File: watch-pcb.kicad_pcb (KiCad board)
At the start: 6 copper layers, 43 x 43 mm, 158 parts, among them J1 DAUGHTER, J2 USB_C_Receptacle, J3 Micro_SD_Card, J4 ELV1411A, J6 TT143AMC12C, U1 ADP2108AUJ-1.8, U10 MAX30102, U11 TPS65631W, U13 LSM6DSV16XTR, U14 LIS3MDL, U15 TXS02612RTW, U16 DRV2605LDGS, U2 TPS63021, U3 STM32H7S7L8H6H, U4 BQ27427YZFR, U5 APS256XXN-OBR-BG, U6 BQ25628E, U7 MX25LM51245GXDI00, U8 APS12808L-3OBMx, U9 TCA9535MRGER, Y1 32.768kHz, Y2 40MHz(10ppm), Y3 32.768kHz, Y4 40MHz(10ppm)

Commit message: no more daughter probably
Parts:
- removed C104, C106: 1uF, Capacitor_SMD:C_0402_1005Metric
- removed C105: 100nF, Capacitor_SMD:C_0402_1005Metric
- removed C52, C89, C90: 10uF, Capacitor_SMD:C_0402_1005Metric
- removed C88: 4.7uF, Capacitor_SMD:C_0402_1005Metric
- removed J4: ELV1411A, custom-lib:ELV1411A
- removed R36, R37: 0, Resistor_SMD:R_0402_1005Metric
- removed R52, R53, R54: 10k, Resistor_SMD:R_0402_1005Metric
- removed R55, R56, R57: R, Resistor_SMD:R_0402_1005Metric
- removed R60: 30.1, Resistor_SMD:R_0402_1005Metric
- removed R61: 5.32k, Resistor_SMD:R_0402_1005Metric
- removed R62: 5k, Resistor_SMD:R_0402_1005Metric
- removed TH2: 103AT-2 10k, Resistor_SMD:R_0603_1608Metric
- removed Y3: 32.768kHz, Crystal:Crystal_SMD_3215-2Pin_3.2x1.5mm
- removed Y4: 40MHz(10ppm), Crystal:Crystal_SMD_3225-4Pin_3.2x2.5mm
- added C19: 1uF, Capacitor_SMD:C_0402_1005Metric, F.Cu at (172.2, 91.1)
- added C20: 2.2uF, Capacitor_SMD:C_0402_1005Metric, F.Cu at (172.2, 93.1)
- added C23: 1uF, Capacitor_SMD:C_0402_1005Metric, F.Cu at (155.5, 56.0)
- added C24: 100nF, Capacitor_SMD:C_0402_1005Metric, F.Cu at (155.5, 57.9)
- added C25: 100nF, Capacitor_SMD:C_0402_1005Metric, F.Cu at (155.5, 59.9)
- added C29: 100nF, Capacitor_SMD:C_0402_1005Metric, F.Cu at (155.5, 67.8)
- added C34: 1uF, Capacitor_SMD:C_0402_1005Metric, F.Cu at (158.4, 63.9)
- added C37: 100nF, Capacitor_SMD:C_0402_1005Metric, F.Cu at (161.2, 56.0)
- added C53: 100nF, Capacitor_SMD:C_0402_1005Metric, F.Cu at (138.6, 55.2)
- added C56: 100nF, Capacitor_SMD:C_0402_1005Metric, F.Cu at (141.5, 45.4)
- added C80: 10uF, Capacitor_SMD:C_0805_2012Metric, F.Cu at (198.9, 91.3)
- added C81: 100nF, Capacitor_SMD:C_0402_1005Metric, F.Cu at (132.2, 95.7)
- added C82: 1uF, Capacitor_SMD:C_0402_1005Metric, F.Cu at (132.2, 97.7)
- added D10: ESD9B3.3ST5G, Diode_SMD:D_SOD-923, F.Cu at (150.1, 47.3)
- added D11: ESD9B3.3ST5G, Diode_SMD:D_SOD-923, F.Cu at (150.1, 49.3)
- added D12: ESD9B3.3ST5G, Diode_SMD:D_SOD-923, F.Cu at (150.1, 51.2)
- added D13: ESD9B3.3ST5G, Diode_SMD:D_SOD-923, F.Cu at (150.1, 53.2)
- added D14: ESD9B3.3ST5G, Diode_SMD:D_SOD-923, F.Cu at (150.1, 55.1)
- added D17: APFA3010, LED_SMD:LED_Kingbright_APFA3010_3x1.5mm_Horizontal, F.Cu at (158.0, 137.2)
- added D8: ESD9B5.0ST5G, Diode_SMD:D_SOD-923, F.Cu at (175.2, 81.0)
- added D9: ESD9B3.3ST5G, Diode_SMD:D_SOD-923, F.Cu at (150.1, 45.4)
- added J5: Micro_SD_Card, Connector_Card:microSD_HC_Molex_104031-0811, F.Cu at (112.4, 163.6)
- added L3: 2.2uH, Inductor_SMD:L_1206_3216Metric, F.Cu at (126.5, 177.0)
- added L4: 2.7nH, Inductor_SMD:L_0201_0603Metric, F.Cu at (178.5, 48.8)
- added R17: 5.1k, Resistor_SMD:R_0402_1005Metric, F.Cu at (166.4, 91.2)
- added R18: 10k, Resistor_SMD:R_0402_1005Metric, F.Cu at (166.4, 93.1)
- added R20: 10k, Resistor_SMD:R_0402_1005Metric, F.Cu at (167.0, 58.0)
- added R21: R, Capacitor_SMD:C_0402_1005Metric, F.Cu at (198.1, 95.8)
- added R22: 10k, Resistor_SMD:R_0402_1005Metric, F.Cu at (167.0, 60.0)
- added R23: 10k, Resistor_SMD:R_0402_1005Metric, F.Cu at (167.0, 62.0)
- added R24: 10k, Resistor_SMD:R_0402_1005Metric, B.Cu at (223.9, 75.6)
- added R25: 499, Resistor_SMD:R_0402_1005Metric, F.Cu at (169.9, 58.0)
- added R26: 0, Resistor_SMD:R_0402_1005Metric, F.Cu at (169.9, 60.0)
- added R27: 0, Resistor_SMD:R_0402_1005Metric, F.Cu at (169.9, 62.0)
- added R28: 0, Resistor_SMD:R_0402_1005Metric, F.Cu at (172.8, 56.0)
- added R29: 0, Resistor_SMD:R_0402_1005Metric, F.Cu at (172.8, 58.0)
- added R30: 0, Resistor_SMD:R_0402_1005Metric, F.Cu at (172.8, 60.0)
- added R46: 10k, Resistor_SMD:R_0402_1005Metric, F.Cu at (141.6, 69.1)
- added TH1: 103AT-2 10k, Resistor_SMD:R_0603_1608Metric, F.Cu at (119.1, 169.5)
- added U12: LSM6DSOXTR, Package_LGA:LGA-14_3x2.5mm_P0.5mm_LayoutBorder3x4y, F.Cu at (125.6, 155.6)
- added U17: KTD2026, Package_DFN_QFN:DFN-8-1EP_1.5x1.5mm_P0.4mm_EP0.7x1.2mm, F.Cu at (120.9, 106.1)
- C1: value 10uF -> 1uF; footprint Capacitor_SMD:C_0603_1608Metric -> Capacitor_SMD:C_0402_1005Metric; moved to F.Cu
- C10: moved to B.Cu
- C11: value 1uF -> 22uF; footprint Capacitor_SMD:C_0402_1005Metric -> Capacitor_SMD:C_0603_1608Metric; moved to B.Cu
- C12: value 100nF -> 4.7uF; footprint Capacitor_SMD:C_0402_1005Metric -> Capacitor_SMD:C_0603_1608Metric; moved to F.Cu
- C13: footprint Capacitor_SMD:C_0402_1005Metric -> Capacitor_SMD:C_0603_1608Metric; moved to F.Cu
- C14: value 1uF -> 10uF; footprint Capacitor_SMD:C_0402_1005Metric -> Capacitor_SMD:C_0603_1608Metric; moved to F.Cu
- C15: value 2.2uF -> 10uF; footprint Capacitor_SMD:C_0402_1005Metric -> Capacitor_SMD:C_0805_2012Metric
- C16: value 47nF -> 10uF; footprint Capacitor_SMD:C_0402_1005Metric -> Capacitor_SMD:C_0603_1608Metric; moved to F.Cu
- C17: value 100nF -> 22uF; footprint Capacitor_SMD:C_0402_1005Metric -> Capacitor_SMD:C_0603_1608Metric; moved to F.Cu
- C18: value 1uF -> 10nF; moved to F.Cu
- C2: value 10uF -> 100nF; footprint Capacitor_SMD:C_0603_1608Metric -> Capacitor_SMD:C_0402_1005Metric; moved to F.Cu
- C21, C22: value C -> 1.5pF; footprint Capacitor_SMD:C_0402_1005Metric -> Capacitor_SMD:C_0201_0603Metric
- C26, C45, C66: value 1uF -> 100nF; moved to F.Cu
- C27, C41: value C -> 1uF
- C28, C42: value C -> 100nF
- C3: value 4.7uF -> 10uF; footprint Capacitor_SMD:C_0402_1005Metric -> Capacitor_SMD:C_0603_1608Metric; moved to F.Cu
- C30, C38, C70, D3, L5, L7, L8, R44: moved to F.Cu
- C31, C47: value 1uF -> C
- C32: value 100nF -> C; moved to F.Cu
- C33: value 1uF -> 10nF
- C36: value 10nF -> 1uF
- C39, C48: value 100nF -> 1uF; moved to F.Cu
- C4: footprint Capacitor_SMD:C_0603_1608Metric -> Capacitor_SMD:C_0402_1005Metric; moved to F.Cu
- C40: value 1uF -> 10uF; moved to F.Cu
- C43: value 10uF -> 100nF; moved to F.Cu
- C44: value 10uF -> 1uF; moved to F.Cu
- C46: value 100nF -> C
- C49: value 10uF -> 4.7uF; footprint Capacitor_SMD:C_0402_1005Metric -> Capacitor_SMD:C_0603_1608Metric
- C5: value 10nF -> 47nF
- C57, C60: value 100nF -> 10uF
- C58: value 4.7uF -> 10uF
- C59, C64, C69: value 1uF -> 100nF
- C6: value 10uF -> 22uF; footprint Capacitor_SMD:C_0402_1005Metric -> Capacitor_SMD:C_0603_1608Metric; moved to F.Cu
- C62: value 10uF -> 1uF
- C63: value 10uF -> 100nF
- C65, C78: value 100nF -> 1uF
- C72: value 100nF -> 10uF; moved to F.Cu
- C73: value 100nF -> 4.7uF; footprint Capacitor_SMD:C_0402_1005Metric -> Capacitor_SMD:C_0603_1608Metric
- C79: value 100nF -> 10uF; footprint Capacitor_SMD:C_0402_1005Metric -> Capacitor_SMD:C_0805_2012Metric; moved to F.Cu
- C9: value 1uF -> 22uF; footprint Capacitor_SMD:C_0402_1005Metric -> Capacitor_SMD:C_0603_1608Metric
- D1: value STATUS1 -> STATUS0
- D15: value STATUS0 -> ESD9B3.3ST5G; footprint LED_SMD:LED_0402_1005Metric -> Diode_SMD:D_SOD-923
- D2: value ESD9B5.0ST5G -> STATUS1; footprint Diode_SMD:D_SOD-923 -> LED_SMD:LED_0402_1005Metric; moved to F.Cu
- D4: value ESD9B5.0ST5G -> CHARGING; footprint Diode_SMD:D_SOD-923 -> LED_SMD:LED_0402_1005Metric; moved to F.Cu
- D5: value ESD9B5.0ST5G -> POWER GOOD; footprint Diode_SMD:D_SOD-923 -> LED_SMD:LED_0402_1005Metric
- D6: value CHARGING -> ESD9B5.0ST5G; footprint LED_SMD:LED_0402_1005Metric -> Diode_SMD:D_SOD-923; moved to F.Cu
- D7: value POWER GOOD -> ESD9B5.0ST5G; footprint LED_SMD:LED_0402_1005Metric -> Diode_SMD:D_SOD-923; moved to F.Cu
- J3: value Micro_SD_Card -> ESP_ANT; footprint Connector_Card:microSD_HC_Molex_104031-0811 -> Connector_Coaxial:U.FL_Molex_MCRF_73412-0110_Vertical
- L2: footprint Inductor_SMD:L_1206_3216Metric -> Inductor_SMD:L_1008_2520Metric; moved to F.Cu
- R10, R8: value 10k -> 1M; moved to B.Cu
- R11: value 5.1k -> 5.32k
- R12: value 5.1k -> 30.1; moved to B.Cu
- R13: value 180k -> R
- R14: value 1M -> R
- R15: value 1M -> 100k; footprint Resistor_SMD:R_0402_1005Metric -> Resistor_SMD:R_0603_1608Metric
- R16: value 22.1k -> 5.1k; moved to F.Cu
- R3: value R -> 10k
- R31, R32: value 10k -> 0; moved to F.Cu
- R33: value 499 -> 0; moved to F.Cu
- R38, R45: value 0 -> 10k
- R39: value R -> 10k; footprint PCM_Resistor_SMD_AKL:R_0402_1005Metric -> Resistor_SMD:R_0402_1005Metric
- R41, R42, R43: value 0 -> 10k; moved to F.Cu
- R5, R6: value 10k -> R
- R7: value 10k -> 180k; moved to B.Cu
- R9: value 10k -> 5k
- U1: value ADP2108AUJ-1.8 -> TPS63021; footprint Package_TO_SOT_SMD:TSOT-23-5 -> custom-lib:Texas_VSON-14_3x4mm_ThermalPad; moved to F.Cu
- U10: value MAX30102 -> LIS3MDL; footprint OptoDevice:Maxim_OLGA-14_3.3x5.6mm_P0.8mm -> Package_LGA:LGA-12_2x2mm_P0.5mm; moved to F.Cu
- U11: value TPS65631W -> LPS22DF; footprint Package_SON:WSON-10-1EP_2.5x2.5mm_P0.5mm_EP1.2x2mm_ThermalVias -> Package_LGA:ST_HLGA-10_2x2mm_P0.5mm_LayoutBorder3x2y
- U13: value LSM6DSV16XTR -> DRV2605LDGS; footprint Package_LGA:LGA-14_3x2.5mm_P0.5mm_LayoutBorder3x4y -> Package_SO:VSSOP-10_3x3mm_P0.5mm
- U14: value LIS3MDL -> MAX30102; footprint Package_LGA:LGA-12_2x2mm_P0.5mm -> OptoDevice:Maxim_OLGA-14_3.3x5.6mm_P0.8mm; moved to B.Cu
- U15: value TXS02612RTW -> SFH9206; footprint Package_DFN_QFN:WQFN-24-1EP_4x4mm_P0.5mm_EP2.45x2.45mm_ThermalVias -> OptoDevice:Osram_SFH9x0x
- U16: value DRV2605LDGS -> LT3465; footprint Package_SO:VSSOP-10_3x3mm_P0.5mm -> Package_TO_SOT_SMD:TSOT-23-6
- U2: value TPS63021 -> BQ25628E; footprint custom-lib:Texas_VSON-14_3x4mm_ThermalPad -> custom-lib:Texas_WQFN-18_2.5x3.0mm_P0.4mm; moved to F.Cu
- U3: value STM32H7S7L8H6H -> TPS62161DSG; footprint Package_BGA:ST_TFBGA-225_13x13mm_Layout15x15_P0.8mm -> Package_SON:WSON-8-1EP_2x2mm_P0.5mm_EP0.9x1.6mm_ThermalVias
- U4: footprint Package_BGA:Texas_DSBGA-9_1.62mmx1.58mm_Layout3x3_P0.5mm -> Package_BGA:Texas_DSBGA-9_1.62x1.58mm_Layout3x3_P0.5mm
- U5: value APS256XXN-OBR-BG -> MX25UM51245GXDI00
- U6: value BQ25628E -> S80KS5123GABHV020; footprint custom-lib:Texas_WQFN-18_2.5x3.0mm_P0.4mm -> custom-lib:BGA-24_6.0x8.0mm_Layout5x5_P1.0mm
- U7: value MX25LM51245GXDI00 -> ESP32-S3; footprint custom-lib:BGA-24_6.0x8.0mm_Layout5x5_P1.0mm -> Package_DFN_QFN:QFN-56-1EP_7x7mm_P0.4mm_EP4x4mm_ThermalVias
- U8: value APS12808L-3OBMx -> TCA9535MRGER; footprint custom-lib:BGA-24_6.0x8.0mm_Layout5x5_P1.0mm -> Package_DFN_QFN:VQFN-24-1EP_4x4mm_P0.5mm_EP2.45x2.45mm; moved to F.Cu
- U9: value TCA9535MRGER -> TPS65631W; footprint Package_DFN_QFN:VQFN-24-1EP_4x4mm_P0.5mm_EP2.45x2.45mm -> Package_SON:WSON-10-1EP_2.5x2.5mm_P0.5mm_EP1.2x2mm_ThermalVias; moved to F.Cu
- moved R7 144.3 mm to (133.0, 175.5), turned to 90 degrees
- moved R10 142.8 mm to (131.0, 175.9), turned to 180 degrees
- moved R8 140.4 mm to (133.0, 173.6), turned to 90 degrees
- moved U3 140.0 mm to (125.4, 174.2), turned to -90 degrees
- moved C45 122.6 mm to (223.4, 76.1), turned to -90 degrees
- moved C17 121.4 mm to (123.4, 175.2), turned to 90 degrees
- moved C6 121.4 mm to (135.2, 174.1), turned to 180 degrees
- moved C11 119.2 mm to (119.0, 172.1), turned to 180 degrees
- moved U1 119.0 mm to (131.6, 174.0), turned to 180 degrees
- moved C16 117.8 mm to (128.1, 175.0), turned to 0 degrees
- moved BT1 117.7 mm to (119.0, 173.8), turned to 180 degrees
- moved C14 117.5 mm to (127.4, 172.8), turned to -90 degrees
- moved L2 115.0 mm to (127.2, 166.9), turned to -90 degrees
- moved C15 114.8 mm to (122.6, 169.9)
- moved D3 114.7 mm to (119.2, 176.9), turned to 0 degrees
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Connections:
- C1 pad 1: +VSW -> VBUS
- C10 pad 1: GND -> +BATT
- C10 pad 2: +3V3 -> GND
- C11 pad 1: GND -> +BATT
- C11 pad 2: +BATT -> GND
- C12 pad 1: +3V3 -> Net-(U2-REGN)
- C12 pad 2: Net-(Q1-C) -> GND
- C13 pad 1: Net-(Q1-C) -> +VSW
- C13 pad 2: +3V3 -> GND
- C14 pad 1: VBUS -> GND
- C14 pad 2: GND -> +VSW
- C15 pad 1: GND -> +BATT
- C15 pad 2: Net-(U4-VDD) -> GND
- C16 pad 1: Net-(U6-BTST) -> +VSW
- C16 pad 2: Net-(U6-SW) -> GND
- C17 pad 1: Net-(U6-PMID) -> +1V8
- C18 pad 1: GND -> VBUS
- C18 pad 2: VBUS -> GND
- C21 pad 1: /STM MCU/CLK_P -> Net-(J3-In)
- C22 pad 1: GND -> /ESP MCU/ESP_ANT
- C22 pad 2: /STM MCU/CLK_M -> GND
- C26 pad 1: Net-(C26-Pad1) -> +1V8
- C27 pad 1: GND -> +1V8
- C27 pad 2: /MCU and Memory/RTC_P -> GND
- C28 pad 1: GND -> +1V8
- C28 pad 2: /MCU and Memory/RTC_N -> GND
- C3 pad 2: +VSW -> Net-(U2-PMID)
- C30 pad 1: +3V3 -> +1V8
- C31 pad 1: +3V3 -> GND
- C31 pad 2: GND -> /ESP MCU/RTC_P
- C32 pad 2: +3V3 -> /ESP MCU/RTC_N
- C35 pad 2: +3V3 -> +1V8
- C36 pad 2: +3V3 -> +1V8
- C38 pad 1: Net-(C38-Pad1) -> +3V3
- C4 pad 1: GND -> Net-(U2-PMID)
- C4 pad 2: +VSW -> GND
- C41 pad 1: Net-(C41-Pad1) -> Net-(U7-CHIP_PU)
- C42 pad 2: /MCU and Memory/CLK_N -> Net-(U7-VDD3P3_CPU)
- C43 pad 1: +3V3 -> GND
- C43 pad 2: GND -> Net-(U7-VDD3P3_CPU)
- C44 pad 1: +3V3 -> GND
- C44 pad 2: GND -> +3V3
- C45 pad 1: Net-(U3A-BOOT0) -> +3V3
- C46 pad 1: +3V3 -> Net-(C46-Pad1)
- C47 pad 1: +3V3 -> GND
- C47 pad 2: GND -> /ESP MCU/CLK_N
- C5 pad 1: VBUS -> Net-(U2-BTST)
- C5 pad 2: GND -> Net-(U2-SW)
- C50 pad 1: +3V3 -> GND
- C50 pad 2: GND -> +3V3
- C54 pad 1: GND -> +3V3
- C54 pad 2: +1V8 -> GND
- C55 pad 2: +1V8 -> +3V3
- C57 pad 1: +3V3 -> GND
- C57 pad 2: GND -> /IO/AMOLED_P
- C58 pad 1: +3V3 -> GND
- C58 pad 2: GND -> /IO/AMOLED_M
- C59 pad 1: +3V3 -> GND
- C59 pad 2: GND -> Net-(U10-C1)
- C6 pad 1: +1V8 -> GND
- C6 pad 2: GND -> +3V3
- C60 pad 1: +3V3 -> GND
- C60 pad 2: GND -> +3V3
- C61 pad 1: +3V3 -> GND
- C61 pad 2: GND -> +3V3
- C62 pad 1: GND -> Net-(C62-Pad1)
- C62 pad 2: /IO/AMOLED_N -> +3V3
- C63 pad 2: /IO/AMOLED_P -> +3V3
- C64 pad 2: GND -> Net-(C62-Pad1)
- C65 pad 1: GND -> +3V3
- C65 pad 2: +3V3 -> GND
- C66 pad 2: GND -> Net-(J6-IOVCC)
- C69 pad 1: +3V3 -> GND
- C69 pad 2: GND -> +3V3
- C71 pad 2: +3V3 -> +VSW
- C72 pad 2: +3V3 -> +1V8
- C73 pad 1: GND -> +3V3
- C73 pad 2: Net-(U14-C1) -> GND
- C74 pad 1: GND -> +3V3
- C74 pad 2: +3V3 -> GND
- C75 pad 1: +3V3 -> +VSW
- C76 pad 1: +3V3 -> GND
- C76 pad 2: GND -> +1V8
- C78 pad 1: +3V3 -> Net-(U13-REG)
- C79 pad 1: +3V3 -> +VSW
- C9 pad 1: Net-(Q1-B) -> +BATT
- D15 pad 2: Net-(D15-A) -> +3V3
- D2 pad 2: /USB and Power/USB_DP -> Net-(D2-A)
- D3 pad 1: VBUS -> GND
- D3 pad 2: GND -> +BATT
- D4 pad 1: GND -> Net-(D4-K)
- D4 pad 2: /USB and Power/USB_DM -> Net-(D4-A)
- D5 pad 1: GND -> Net-(D5-K)
- D5 pad 2: +BATT -> Net-(D5-A)
- D6 pad 1: Net-(D6-K) -> VBUS
- D6 pad 2: Net-(D6-A) -> GND
- D7 pad 1: Net-(D7-K) -> GND
- D7 pad 2: Net-(D7-A) -> /USB and Power/USB_DP
- J1 pad 10: /MCU and Memory/EXT_IO9 -> unconnected-(J1-Pin_10-Pad10)
- J1 pad 6: /MCU and Memory/IO6 -> unconnected-(J1-Pin_6-Pad6)
- J1 pad 7: /MCU and Memory/IO7 -> unconnected-(J1-Pin_7-Pad7)
- J1 pad 8: /MCU and Memory/EXT_IO7 -> unconnected-(J1-Pin_8-Pad8)
- J1 pad 9: /MCU and Memory/EXT_IO8 -> unconnected-(J1-Pin_9-Pad9)
- J3 pad 1: /STM MCU/SD_DEV_D2 -> Net-(J3-In)
- J3 pad 2: /STM MCU/SD_DEV_D3 -> GND
- J6 pad 11: /IO/DISP_CLK -> /ESP MCU/FSPI_CLK
- J6 pad 13: /IO/DISP_D1 -> /ESP MCU/FSPI_Q
- J6 pad 14: /IO/DISP_D2 -> /ESP MCU/FSPI_WP
- J6 pad 19: +3V3 -> Net-(J6-IOVCC)
- J6 pad 20: +3V3 -> Net-(C62-Pad1)
- J6 pad 23: /IO/AMOLED_N -> /IO/AMOLED_M
- J6 pad 24: GND -> Net-(J6-MTP_PWR)
- J6 pad 3: /IO/SI2C_SDA -> /IO/TP_SDA
- J6 pad 4: /IO/SI2C_SCL -> /IO/TP_SCL
- J6 pad 7: /IO/DISP_CS -> /ESP MCU/FSPI_CS
- J6 pad 8: /IO/DISP_D0 -> /ESP MCU/FSPI_D
- J6 pad 9: /IO/DISP_D3 -> /ESP MCU/FSPI_HD
- JP1 pad 2: /MCU and Memory/EN -> /ESP MCU/EN
- L2 pad 1: Net-(U1-SW) -> Net-(U2-SW)
- L2 pad 2: +1V8 -> +VSW
- L5 pad 1: Net-(C38-Pad1) -> Net-(U7-VDD3P3)
- L6 pad 1: Net-(C41-Pad1) -> Net-(C46-Pad1)
- L6 pad 2: /MCU and Memory/CLK_P -> /ESP MCU/CLK_P
- L7 pad 1: GND -> +3V3
- L7 pad 2: Net-(U11-SWN) -> Net-(U9-SWP)
- L8 pad 1: +3V3 -> GND
- L8 pad 2: Net-(U11-SWP) -> Net-(U9-SWN)
- MK2 pad 2: +3V3 -> +1V8
- R1 pad 1: /MCU and Memory/EXT_IO12 -> unconnected-(R1-Pad1)
- R10 pad 1: /IMU_SCL_PU -> +3V3
- R10 pad 2: +3V3 -> /USB and Power/3V3_GOOD
- R11 pad 1: Net-(J2-CC1) -> Net-(U2-TS)
- R11 pad 2: GND -> Net-(U2-TS_BIAS)
- R12 pad 1: Net-(J2-CC2) -> GND
- R12 pad 2: GND -> Net-(U2-TS)
- R13 pad 1: GND -> Net-(D4-A)
- R13 pad 2: Net-(U2-FB) -> +3V3
- R14 pad 1: Net-(U2-FB) -> Net-(D5-A)
- R15 pad 1: +3V3 -> +1V8
- R15 pad 2: /MCU and Memory/EXT_IO14 -> /USB and Power/1V8_GOOD
- R16 pad 1: Net-(Q1-B) -> Net-(J2-CC1)
- R16 pad 2: VBUS -> GND
- R19 pad 1: GND -> +1V8
- R19 pad 2: Net-(U4-BIN) -> Net-(U6-RST#)
- R2 pad 1: /MCU and Memory/EXT_IO13 -> unconnected-(R2-Pad1)
- R3 pad 1: Net-(D1-A) -> unconnected-(R3-Pad1)
- R3 pad 2: /MCU and Memory/EXT_IO11 -> +3V3
- R31 pad 1: /MCU and Memory/EN -> /ESP MCU/MEM_D7
- R31 pad 2: +3V3 -> Net-(U7-GPIO36)
- R32 pad 1: /MCU and Memory/EN -> /ESP MCU/MEM_CLK
- R32 pad 2: Net-(C26-Pad1) -> Net-(U7-SPICLK)
- R33 pad 1: /MCU and Memory/TX -> /ESP MCU/MEM_DQS
- R33 pad 2: unconnected-(R33-Pad2) -> Net-(U7-GPIO37)
- R34 pad 1: /MCU and Memory/MEM_D3 -> /ESP MCU/MEM_D1
- R34 pad 2: unconnected-(R34-Pad2) -> Net-(U7-SPIQ)
- R35 pad 1: /MCU and Memory/MEM_D2 -> /ESP MCU/MEM_D0
- R35 pad 2: unconnected-(R35-Pad2) -> Net-(U7-SPID)
- R38 pad 1: /MCU and Memory/MEM_D0 -> +3V3
- R38 pad 2: unconnected-(R38-Pad2) -> /IO/SD_D2
- R39 pad 1: /MCU and Memory/RTC_P -> +3V3
- R39 pad 2: /MCU and Memory/RTC_N -> /IO/SD_D3
- R40 pad 2: /MCU and Memory/FLASH_RST -> /IO/SD_CMD
- R41 pad 1: /MCU and Memory/MEM_D4 -> +3V3
- R41 pad 2: unconnected-(R41-Pad2) -> /IO/SD_CLK
- R42 pad 1: /MCU and Memory/MEM_D5 -> +3V3
- R42 pad 2: unconnected-(R42-Pad2) -> /IO/SD_D0
- R43 pad 1: /MCU and Memory/MEM_D6 -> +3V3
- R43 pad 2: unconnected-(R43-Pad2) -> /IO/SD_D1
- R44 pad 1: /MCU and Memory/MEM_D7 -> GND
- R44 pad 2: unconnected-(R44-Pad2) -> Net-(J6-MTP_PWR)
- R45 pad 1: /MCU and Memory/MEM_DQS -> GND
- R45 pad 2: unconnected-(R45-Pad2) -> /IO/MIC_SD
- R5 pad 1: unconnected-(R5-Pad1) -> Net-(D1-A)
- R5 pad 2: +3V3 -> unconnected-(R5-Pad2)
- R6 pad 1: unconnected-(R6-Pad1) -> Net-(D2-A)
- R6 pad 2: +3V3 -> unconnected-(R6-Pad2)
- R7 pad 1: unconnected-(R7-Pad1) -> GND
- R7 pad 2: +3V3 -> Net-(U1-FB)
- R8 pad 1: unconnected-(R8-Pad1) -> Net-(U1-FB)
- R9 pad 1: /IMU_SDA_PU -> /USB and Power/ILIM
- R9 pad 2: +3V3 -> GND
- U1 pad 3: +VSW -> Net-(U1-FB)
- U1 pad 4: +1V8 -> +3V3
- U1 pad 5: Net-(U1-SW) -> +3V3
- U10 pad 1: unconnected-(U10-NC-Pad1) -> /IO/MAG_SCL
- U10 pad 11: +1V8 -> /IO/MAG_SDA
- U10 pad 2: /IO/IMU_SCL -> GND
- U10 pad 3: /IO/IMU_SDA -> GND
- U10 pad 4: GND -> Net-(U10-C1)
- U10 pad 5: unconnected-(U10-NC-Pad5) -> +3V3
- U10 pad 6: unconnected-(U10-NC-Pad6) -> +3V3
- U10 pad 7: unconnected-(U10-NC-Pad7) -> /IO/MAG_INT
- U10 pad 8: unconnected-(U10-NC-Pad8) -> /IO/MAG_DRDY
- U10 pad 9: +3V3 -> GND
- U11 pad 1: Net-(U11-SWP) -> +3V3
- U11 pad 2: GND -> /IO/ALT_SCL
- U11 pad 3: /IO/AMOLED_P -> GND
- U11 pad 4: /IO/AMOLED_P -> /IO/ALT_SDA
- U11 pad 6: /IO/SWIRE -> +1V8
- U11 pad 7: /IO/AMOLED_N -> /IO/ALT_DRDY
- U11 pad 8: Net-(U11-SWN) -> GND
- U11 pad 9: +3V3 -> GND
- U13 pad 1: GND -> Net-(U13-REG)
- U13 pad 10: unconnected-(U13-OCS_AUX-Pad10) -> +VSW
- U13 pad 2: unconnected-(U13-SDx/AH1/QVAR1-Pad2) -> /IO/MTR_SCL
- U13 pad 3: unconnected-(U13-SCx/AH2/QVAR2-Pad3) -> /IO/MTR_SDA
- U13 pad 4: /IO/IMU_INT1 -> GND
- U13 pad 5: +3V3 -> /IO/MTR_EN
- U13 pad 6: GND -> +VSW
- U13 pad 7: GND -> /IO/MTR_P
- U13 pad 8: +3V3 -> GND
- U13 pad 9: /IO/IMU_INT2 -> /IO/MTR_N
- U14 pad 1: /IO/IMU_SCL -> unconnected-(U14-NC-Pad1)
- U14 pad 11: /IO/IMU_SDA -> +1V8
- U14 pad 2: GND -> /IO/HBT_SCL
- U14 pad 3: GND -> /IO/HBT_SDA
- U14 pad 4: Net-(U14-C1) -> GND
- U14 pad 5: +3V3 -> unconnected-(U14-NC-Pad5)
- U14 pad 6: +3V3 -> unconnected-(U14-NC-Pad6)
- U14 pad 7: /IO/MAG_INT -> unconnected-(U14-NC-Pad7)
- U14 pad 8: /IO/MAG_DRDY -> unconnected-(U14-NC-Pad8)
- U14 pad 9: GND -> +3V3
- U15 pad 1: /STM MCU/SD_HOST_D2 -> unconnected-(U15-A-Pad1)
- U15 pad 2: GND -> unconnected-(U15-NC-Pad2)
- U15 pad 3: /STM MCU/SD_HOST_D3 -> unconnected-(U15-E-Pad3)
- U15 pad 4: /STM MCU/SD_HOST_CMD -> unconnected-(U15-C-Pad4)
- U15 pad 5: +3V3 -> unconnected-(U15-NC-Pad5)
- U15 pad 6: /STM MCU/SD_HOST_D0 -> unconnected-(U15-K-Pad6)
- U16 pad 1: Net-(U16-REG) -> unconnected-(U16-VOUT-Pad1)
- U16 pad 2: /IO/SI2C_SCL -> unconnected-(U16-GND-Pad2)
- U16 pad 3: /IO/SI2C_SDA -> unconnected-(U16-FB-Pad3)
- U16 pad 4: GND -> unconnected-(U16-CTRL-Pad4)
- U16 pad 5: /IO/MTR_EN -> unconnected-(U16-VIN-Pad5)
- U16 pad 6: +3V3 -> unconnected-(U16-SW-Pad6)
- U2 pad 1: +VSW -> Net-(U2-BTST)
- U2 pad 10: +VSW -> Net-(D4-K)
- U2 pad 11: +VSW -> /USB and Power/CHARGE_INT
- U2 pad 12: +VSW -> /USB and Power/SDA
- U2 pad 13: /MCU and Memory/EXT_IO5 -> /USB and Power/SCL
- U2 pad 14: /MCU and Memory/EXT_IO14 -> GND
- U2 pad 2: GND -> Net-(U2-REGN)
- U2 pad 3: Net-(U2-FB) -> Net-(D5-K)
- U2 pad 4: +3V3 -> /USB and Power/ILIM
- U2 pad 5: +3V3 -> Net-(U2-TS_BIAS)
- U2 pad 6: Net-(L1-Pad2) -> Net-(U2-TS)
- U2 pad 7: Net-(L1-Pad2) -> /USB and Power/POWER_BTN
- U2 pad 8: Net-(L1-Pad1) -> +BATT
- U2 pad 9: Net-(L1-Pad1) -> +VSW
- U4 pad A1: /MCU and Memory/EXT_IO12 -> /USB and Power/BAT_LOW
- U4 pad A2: /SI2C_SDA -> /USB and Power/SDA
- U4 pad A3: /SI2C_SCL -> /USB and Power/SCL
- U5 pad A2: /STM MCU/RAM_D10 -> unconnected-(U5-NC-PadA2)
- U5 pad A3: /STM MCU/RAM_CS -> unconnected-(U5-NC-PadA3)
- U5 pad A4: /STM MCU/RAM_D11 -> Net-(U5-RESET#)
- U5 pad A5: /STM MCU/RAM_D12 -> unconnected-(U5-ECS#-PadA5)
- U5 pad B1: /STM MCU/RAM_D9 -> unconnected-(U5-DNU-PadB1)
- U5 pad B2: /STM MCU/RAM_CLK -> /ESP MCU/MEM_CLK
- U5 pad B3: /STM MCU/RAM_DQS1 -> GND
- U5 pad B4: /STM MCU/RAM_D13 -> +1V8
- U5 pad B5: /STM MCU/RAM_D14 -> unconnected-(U5-DNU-PadB5)
- U5 pad C2: /STM MCU/RAM_D8 -> /ESP MCU/MEM_CS0
- U5 pad C3: /STM MCU/RAM_DQS0 -> /ESP MCU/MEM_DQS
- U5 pad C4: /STM MCU/RAM_D2 -> /ESP MCU/MEM_D2
- U5 pad C5: /STM MCU/RAM_D15 -> unconnected-(U5-NC-PadC5)
- U5 pad D2: /STM MCU/RAM_D1 -> /ESP MCU/MEM_D1
- U5 pad D3: /STM MCU/RAM_D0 -> /ESP MCU/MEM_D0
- U5 pad D4: /STM MCU/RAM_D3 -> /ESP MCU/MEM_D3
- U5 pad D5: /STM MCU/RAM_D4 -> /ESP MCU/MEM_D4
- U5 pad E1: /STM MCU/RAM_D7 -> /ESP MCU/MEM_D7
- U5 pad E2: /STM MCU/RAM_D6 -> /ESP MCU/MEM_D6
- U5 pad E3: /STM MCU/RAM_D5 -> /ESP MCU/MEM_D5
- U9 pad 1: /MCU and Memory/FLASH_RST -> Net-(U9-SWP)
- U9 pad 10: /MCU and Memory/EXT_IO7 -> +3V3
- U9 pad 11: /MCU and Memory/EXT_IO8 -> GND
- U9 pad 2: /MCU and Memory/RAM_RST -> GND
- U9 pad 3: /MCU and Memory/EXT_IO1 -> /IO/AMOLED_P
- U9 pad 4: /MCU and Memory/EXT_IO2 -> /IO/AMOLED_P
- U9 pad 5: /MCU and Memory/EXT_IO3 -> GND
- U9 pad 6: /MCU and Memory/EXT_IO4 -> /IO/SWIRE
- U9 pad 7: /MCU and Memory/EXT_IO5 -> /IO/AMOLED_M
- U9 pad 8: /MCU and Memory/EXT_IO6 -> Net-(U9-SWN)
- U9 pad 9: GND -> +3V3
- Y1 pad 1: /MCU and Memory/RTC_N -> /ESP MCU/RTC_N
- Y1 pad 2: /MCU and Memory/RTC_P -> /ESP MCU/RTC_P
- Y2 pad 1: Net-(C41-Pad1) -> Net-(C46-Pad1)
- Y2 pad 3: /MCU and Memory/CLK_N -> /ESP MCU/CLK_N
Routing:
- net +3V3: track 217.1 -> 0.00 mm, vias 39 -> 0
- net unconnected-(J4-Pin_3-Pad3): track 158.2 -> 0.00 mm, vias 13 -> 0
- net (no net): track 124.2 -> 0.00 mm, vias 22 -> 0
- net +VSW: track 66.3 -> 0.00 mm, vias 14 -> 0
- net Net-(Q1-B): track 43.7 -> 0.00 mm, vias 2 -> 0
- net /MCU and Memory/EN: track 39.2 -> 0.00 mm, vias 2 -> 0
- net /MCU and Memory/EXT_IO14: track 37.2 -> 0.00 mm, vias 4 -> 0
- net /USB and Power/USB_DM: track 36.3 -> 0.00 mm, vias 2 -> 0
- net /MCU and Memory/SD_CLK: track 33.6 -> 0.00 mm, vias 2 -> 0
- net +1V8: track 33.3 -> 0.00 mm, vias 2 -> 0
- net /IO/MAG_DRDY: track 33.0 -> 0.00 mm, vias 2 -> 0
- net /USB and Power/USB_DP: track 32.9 -> 0.00 mm, vias 2 -> 0
- net /IO/MAG_INT: track 32.3 -> 0.00 mm, vias 2 -> 0
- net /USB and Power/ILIM: track 31.9 -> 0.00 mm, vias 6 -> 0
- net /IO/MIC_SD: track 29.9 -> 0.00 mm, vias 3 -> 0
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- removed copper zone on B.Cu, net GND
- removed copper zone on F.Cu, net GND
- removed copper zone on In1.Cu, net GND
- removed copper zone on In2.Cu, net GND
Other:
- board size 43 x 43 mm -> 47 x 41.8 mm

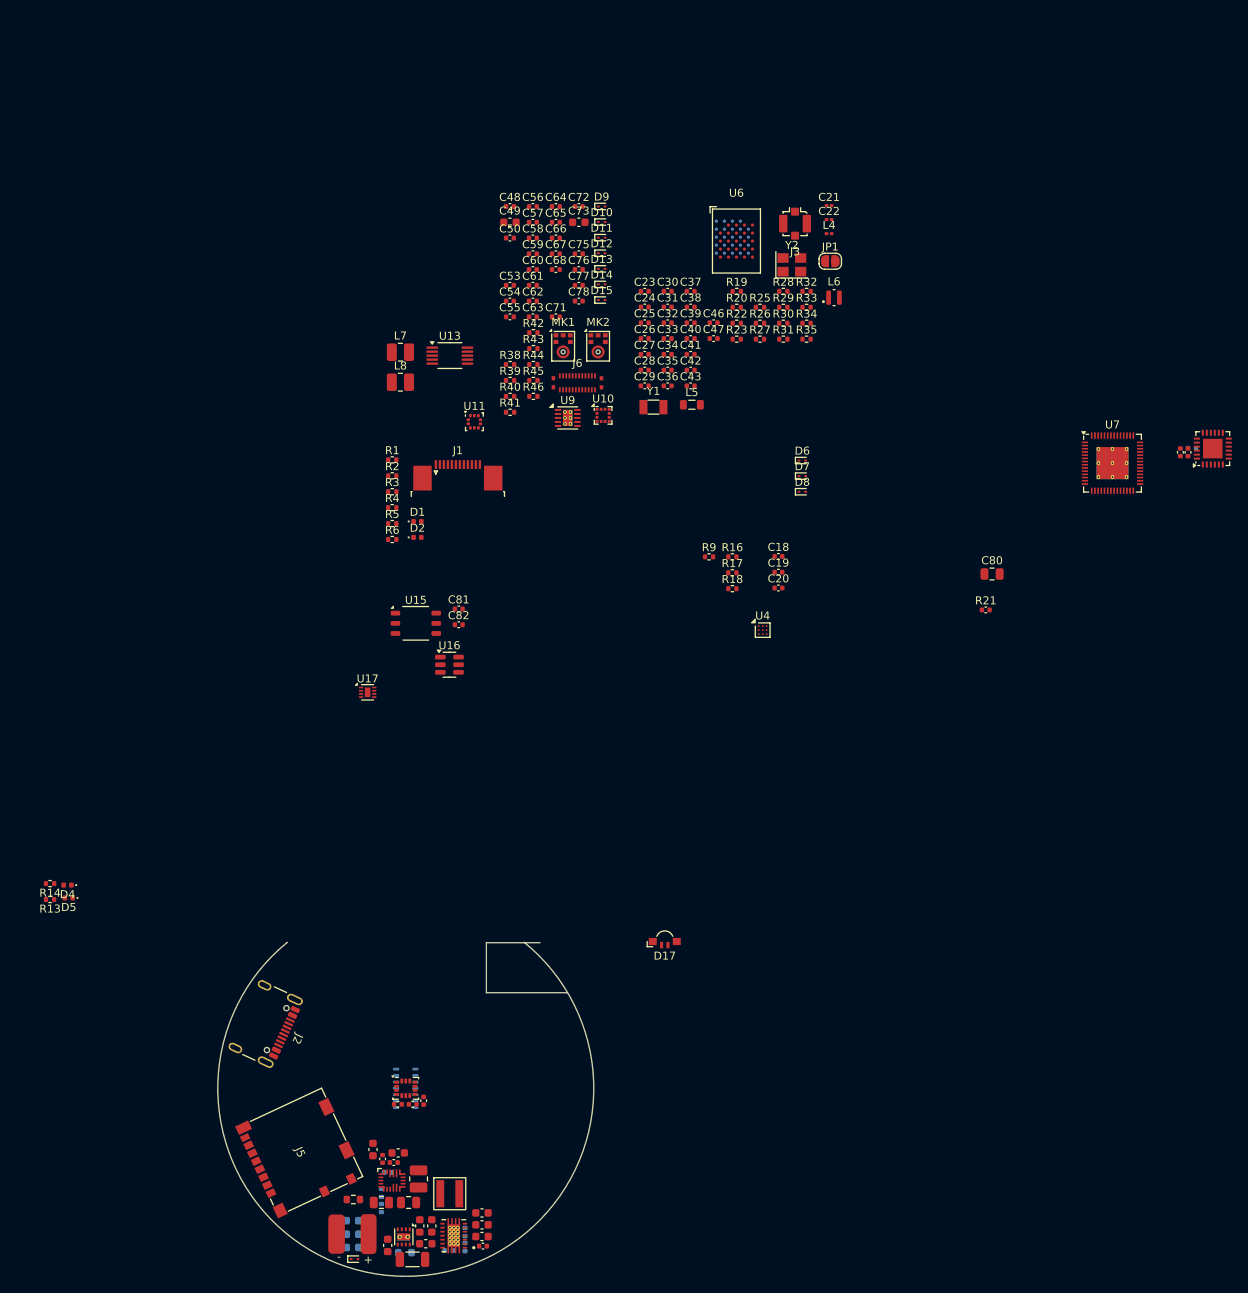
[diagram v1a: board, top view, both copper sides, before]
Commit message: basically done with board layout, gonna try to do a smaller one (47->42mm diameter)
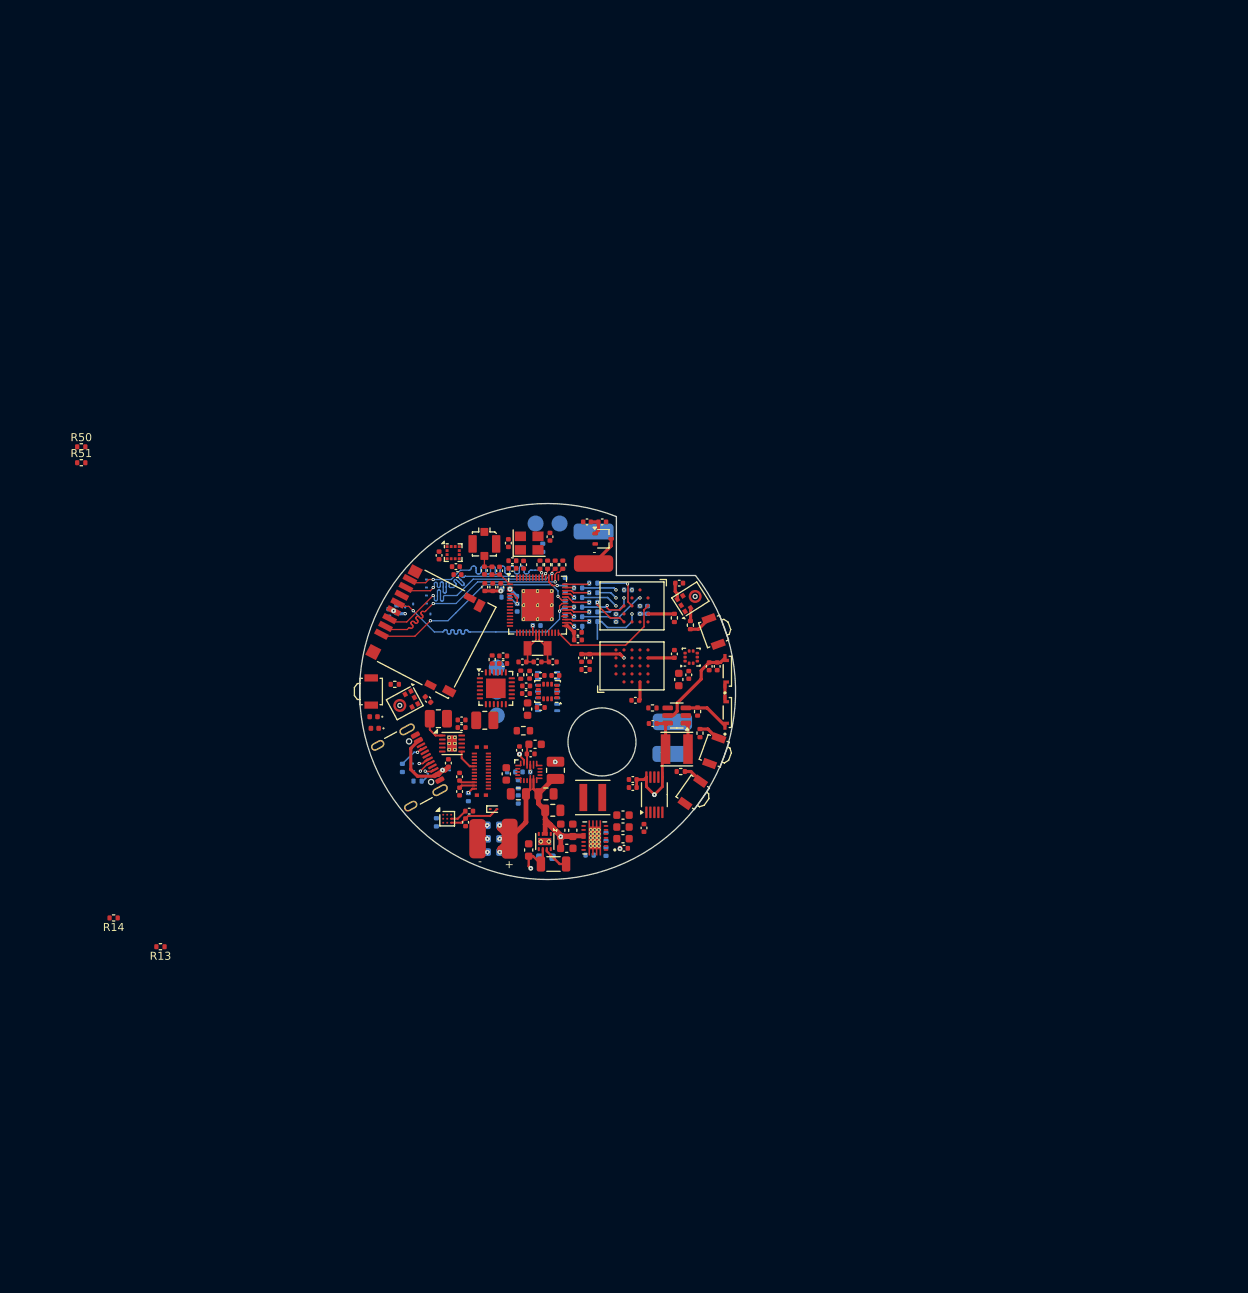
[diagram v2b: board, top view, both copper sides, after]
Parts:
- removed C54, C63, C64, C66, C81: 100nF, Capacitor_SMD:C_0402_1005Metric
- removed C62, C65: 1uF, Capacitor_SMD:C_0402_1005Metric
- removed D17: APFA3010, LED_SMD:LED_Kingbright_APFA3010_3x1.5mm_Horizontal
- removed JP1: RESET=LOW, Jumper:SolderJumper-2_P1.3mm_Open_RoundedPad1.0x1.5mm
- removed R1, R2, R22, R3: 10k, Resistor_SMD:R_0402_1005Metric
- removed R35: 0, Resistor_SMD:R_0402_1005Metric
- removed U15: SFH9206, OptoDevice:Osram_SFH9x0x
- removed U17: KTD2026, Package_DFN_QFN:DFN-8-1EP_1.5x1.5mm_P0.4mm_EP0.7x1.2mm
- added C51: 1uF, Capacitor_SMD:C_0402_1005Metric, F.Cu at (156.5, 110.0)
- added C83: 100nF, Capacitor_SMD:C_0402_1005Metric, F.Cu at (163.6, 102.8)
- added J4: LASER, custom-lib:LASER_connector, B.Cu at (149.1, 88.0)
- added L9: NRS4018T220MDGJ, Inductor_SMD:L_Taiyo-Yuden_MD-4040, F.Cu at (159.5, 113.2)
- added Q1: BSS214NW, Package_TO_SOT_SMD:SOT-323_SC-70, F.Cu at (150.3, 86.9)
- added R36: 1k, Capacitor_SMD:C_0402_1005Metric, F.Cu at (148.3, 84.8)
- added R37: 10k, Capacitor_SMD:C_0402_1005Metric, F.Cu at (150.2, 84.8)
- added R47: 10k, Resistor_SMD:R_0402_1005Metric, F.Cu at (161.2, 97.7)
- added R48: 10k, Resistor_SMD:R_0402_1005Metric, F.Cu at (162.4, 111.2)
- added R49: 10k, Resistor_SMD:R_0402_1005Metric, F.Cu at (160.0, 116.0)
- added R50: 10k, Resistor_SMD:R_0402_1005Metric, F.Cu at (85.1, 75.4)
- added R51: 10k, Resistor_SMD:R_0402_1005Metric, F.Cu at (85.1, 77.4)
- added SW1: B3U-3000P, Button_Switch_SMD:SW_SPST_B3U-3000P, F.Cu at (121.3, 106.0)
- added SW3: SW_Push, Button_Switch_SMD:SW_SPST_B3U-3000P, F.Cu at (164.1, 98.5)
- added SW4: SW_Push, Button_Switch_SMD:SW_SPST_B3U-3000P, F.Cu at (164.2, 113.4)
- added SW5: SW_Push, Button_Switch_SMD:SW_SPST_B3U-3000P, F.Cu at (161.5, 118.6)
- added TP1: BOOT, TestPoint:TestPoint_Pad_D2.0mm, B.Cu at (137.0, 103.0)
- added TP2: RST, TestPoint:TestPoint_Pad_D2.0mm, B.Cu at (137.0, 109.0)
- added TP3: GND, TestPoint:TestPoint_Pad_D2.0mm, B.Cu at (137.0, 106.0)
- added TP4: RX, TestPoint:TestPoint_Pad_D2.0mm, B.Cu at (141.8, 85.0)
- added TP5: TX, TestPoint:TestPoint_Pad_D2.0mm, B.Cu at (144.8, 85.0)
- C21, C22: footprint Capacitor_SMD:C_0201_0603Metric -> Capacitor_SMD:C_0402_1005Metric
- C27, C28, C29, C30, C37, C41, C42, C43, C60, C61, D10, D11, D12, D13, D14, D15, D6, D7, D8, D9, R16, R17, R18, R23, R25, R26, R27, R28, R29, R30, R31, R32, R33, R38, R41, R44, R9: moved to B.Cu
- C72: value 10uF -> 1uF
- C82: value 1uF -> 100nF
- D1: value STATUS0 -> CUW Y3SH.B2-JD-42-6T; footprint LED_SMD:LED_0402_1005Metric -> custom-lib:LED_CUW_Y3SH.B2-GFJD-5J6T-Z242-20-R18-Z
- D2: value STATUS1 -> CUW Y3SH.B2-JD-42-6T; footprint LED_SMD:LED_0402_1005Metric -> custom-lib:LED_CUW_Y3SH.B2-GFJD-5J6T-Z242-20-R18-Z
- J1: value DAUGHTER -> NFP-ELV0832B; footprint Connector_FFC-FPC:TE_1-1734839-2_1x12-1MP_P0.5mm_Horizontal -> custom-lib:Battery_Connector; moved to B.Cu
- J5: footprint Connector_Card:microSD_HC_Molex_104031-0811 -> Connector_Card:microSD_HC_Hirose_DM3D-SF
- L1: value 1.5uH -> XFL4020-152ME; footprint custom-lib:XFL4020-152ME -> Inductor_SMD:L_Coilcraft_XxL4040
- L4: footprint Inductor_SMD:L_0201_0603Metric -> Inductor_SMD:L_0402_1005Metric
- L5: footprint Inductor_SMD:L_0805_2012Metric -> Inductor_SMD:L_0402_1005Metric; moved to B.Cu
- L6: footprint Inductor_SMD:L_Coilcraft_XFL2010 -> Capacitor_SMD:C_0402_1005Metric
- R24, U5: moved to F.Cu
- R34: value 0 -> 10k
- R4: value 10k -> 5
- R5, R6: value R -> 0; moved to B.Cu
- U16: value LT3465 -> AP3019AK; footprint Package_TO_SOT_SMD:TSOT-23-6 -> Package_TO_SOT_SMD:SOT-23-6
- moved U8 94.5 mm to (136.9, 105.6), turned to 0 degrees
- moved R24 91.4 mm to (136.4, 102.0), turned to 90 degrees
- moved C45 89.6 mm to (137.8, 102.5), turned to 0 degrees
- moved C44 88.4 mm to (137.8, 101.5), turned to 180 degrees
- moved U7 74.0 mm to (142.1, 95.2)
- moved C57 69.9 mm to (132.3, 116.7), turned to -90 degrees
- moved C58 69.8 mm to (132.3, 118.5), turned to 90 degrees
- moved J5 67.1 mm to (128.8, 98.5), turned to -117.5 degrees
- moved C75 67.1 mm to (154.0, 118.0), turned to 180 degrees
- moved C78 66.4 mm to (155.4, 123.0), turned to -90 degrees
- moved C56 64.8 mm to (132.6, 109.5), turned to 180 degrees
- moved C21 62.7 mm to (135.4, 90.9), turned to -90 degrees
- moved C80 62.4 mm to (144.0, 120.8)
- moved TH1 62.3 mm to (140.3, 110.9)
- moved C72 61.2 mm to (140.7, 106.2)
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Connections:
- net /USB and Power/ILIM renamed Net-(U2-ILIM)
- C15 pad 1: +BATT -> GND
- C15 pad 2: GND -> +BATT
- C24 pad 1: +1V8 -> GND
- C24 pad 2: GND -> +1V8
- C42 pad 2: Net-(U7-VDD3P3_CPU) -> +3V3
- C43 pad 2: Net-(U7-VDD3P3_CPU) -> +3V3
- C82 pad 1: +3V3 -> Net-(D1-A)
- D1 pad 1: GND -> Net-(D1-K)
- D10 pad 2: /IO/SD_D3 -> /ESP MCU/SD_D3
- D11 pad 2: /IO/SD_CMD -> /ESP MCU/SD_CMD
- D12 pad 2: /IO/SD_CLK -> /ESP MCU/SD_CLK
- D13 pad 2: /IO/SD_D0 -> /ESP MCU/SD_D0
- D14 pad 2: /IO/SD_D1 -> /ESP MCU/SD_D1
- D2 pad 1: GND -> Net-(D2-K)
- D2 pad 2: Net-(D2-A) -> Net-(D1-K)
- D9 pad 2: /IO/SD_D2 -> /ESP MCU/SD_D2
- J1 pad 1: +3V3 -> Net-(J1-Pin_1)
- J1 pad 2: +3V3 -> Net-(J1-Pin_2)
- J5 pad 1: /IO/SD_D2 -> /ESP MCU/SD_D2
- J5 pad 2: /IO/SD_D3 -> /ESP MCU/SD_D3
- J5 pad 3: /IO/SD_CMD -> /ESP MCU/SD_CMD
- J5 pad 5: /IO/SD_CLK -> /ESP MCU/SD_CLK
- J5 pad 7: /IO/SD_D0 -> /ESP MCU/SD_D0
- J5 pad 8: /IO/SD_D1 -> /ESP MCU/SD_D1
- J6 pad 19: Net-(J6-IOVCC) -> +3V3
- J6 pad 20: Net-(C62-Pad1) -> +3V3
- MK2 pad 2: +1V8 -> +3V3
- R25 pad 1: /ESP MCU/TX -> /ESP MCU/IO8
- R26 pad 1: /ESP MCU/MEM_D3 -> Net-(U7-GPIO35)
- R26 pad 2: Net-(U7-SPIHD) -> /ESP MCU/MEM_D6
- R27 pad 1: /ESP MCU/MEM_D4 -> Net-(U7-GPIO36)
- R27 pad 2: Net-(U7-GPIO33) -> /ESP MCU/MEM_D7
- R28 pad 1: /ESP MCU/MEM_D2 -> Net-(U7-GPIO37)
- R28 pad 2: Net-(U7-SPIWP) -> /ESP MCU/MEM_DQS
- R29 pad 1: /ESP MCU/MEM_D5 -> /ESP MCU/MEM_D3
- R29 pad 2: Net-(U7-GPIO34) -> Net-(U7-SPIHD)
- R30 pad 1: /ESP MCU/MEM_D6 -> /ESP MCU/MEM_D2
- R30 pad 2: Net-(U7-GPIO35) -> Net-(U7-SPIWP)
- R31 pad 1: /ESP MCU/MEM_D7 -> /ESP MCU/MEM_CLK
- R31 pad 2: Net-(U7-GPIO36) -> Net-(U7-SPICLK)
- R32 pad 1: /ESP MCU/MEM_CLK -> /ESP MCU/MEM_D1
- R32 pad 2: Net-(U7-SPICLK) -> Net-(U7-SPIQ)
- R33 pad 1: /ESP MCU/MEM_DQS -> /ESP MCU/MEM_D0
- R33 pad 2: Net-(U7-GPIO37) -> Net-(U7-SPID)
- R34 pad 1: /ESP MCU/MEM_D1 -> /IO/LIGHT
- R34 pad 2: Net-(U7-SPIQ) -> GND
- R38 pad 2: /IO/SD_D2 -> /ESP MCU/SD_D2
- R39 pad 2: /IO/SD_D3 -> /ESP MCU/SD_D3
- R4 pad 1: unconnected-(R4-Pad1) -> Net-(D2-K)
- R4 pad 2: +3V3 -> GND
- R40 pad 2: /IO/SD_CMD -> /ESP MCU/SD_CMD
- R41 pad 2: /IO/SD_CLK -> /ESP MCU/SD_CLK
- R42 pad 2: /IO/SD_D0 -> /ESP MCU/SD_D0
- R43 pad 2: /IO/SD_D1 -> /ESP MCU/SD_D1
- R5 pad 1: Net-(D1-A) -> Net-(U7-GPIO33)
- R5 pad 2: unconnected-(R5-Pad2) -> /ESP MCU/MEM_D4
- R6 pad 1: Net-(D2-A) -> Net-(U7-GPIO34)
- R6 pad 2: unconnected-(R6-Pad2) -> /ESP MCU/MEM_D5
- U11 pad 6: +1V8 -> +3V3
- U13 pad 7: /IO/MTR_P -> Net-(J1-Pin_1)
- U13 pad 9: /IO/MTR_N -> Net-(J1-Pin_2)
- U16 pad 1: unconnected-(U16-VOUT-Pad1) -> Net-(U16-SW)
- U16 pad 2: unconnected-(U16-GND-Pad2) -> GND
- U16 pad 3: unconnected-(U16-FB-Pad3) -> Net-(D2-K)
- U16 pad 4: unconnected-(U16-CTRL-Pad4) -> /IO/LIGHT
- U16 pad 5: unconnected-(U16-VIN-Pad5) -> Net-(D1-A)
- U16 pad 6: unconnected-(U16-SW-Pad6) -> +VSW
- U2 pad 7: /USB and Power/POWER_BTN -> Net-(U2-QON)
- U7 pad 20: Net-(U7-VDD3P3_CPU) -> +3V3
- U7 pad 25: /ESP MCU/IO8 -> /ESP MCU/USB_DM
- U7 pad 26: /ESP MCU/IO9 -> /ESP MCU/USB_DP
- U7 pad 37: /ESP MCU/SD_CMD -> /ESP MCU/SD_D2
- U7 pad 44: /ESP MCU/SD_D0 -> /ESP MCU/SD_D3
- U7 pad 45: /ESP MCU/SD_D1 -> /ESP MCU/SD_CMD
- U7 pad 46: Net-(U7-VDD3P3_CPU) -> +3V3
- U7 pad 47: /ESP MCU/SD_D2 -> /ESP MCU/SD_D0
- U7 pad 48: /ESP MCU/SD_D3 -> /ESP MCU/SD_D1
- U7 pad 50: /ESP MCU/RX -> /ESP MCU/IO9
- U7 pad 51: /ESP MCU/I2S_SCK -> /ESP MCU/I2S_WS
- U7 pad 52: /ESP MCU/BOOTSEL -> /ESP MCU/I2S_SCK
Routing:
- net +VSW: track 0.00 -> 55.0 mm, vias 0 -> 3
- net /ESP MCU/SD_D3: track 0.00 -> 28.6 mm, vias 0 -> 2
- net /ESP MCU/SD_CLK: track 0.00 -> 28.5 mm, vias 0 -> 2
- net /ESP MCU/SD_D2: track 0.00 -> 28.1 mm, vias 0 -> 2
- net /ESP MCU/SD_CMD: track 0.00 -> 27.8 mm, vias 0 -> 2
- net /ESP MCU/SD_D0: track 0.00 -> 27.7 mm, vias 0 -> 2
- net /ESP MCU/SD_D1: track 0.00 -> 27.4 mm, vias 0 -> 2
- net VBUS: track 0.00 -> 21.3 mm, vias 0 -> 2
- net +BATT: track 0.00 -> 20.6 mm, vias 0 -> 3
- net +1V8: track 0.00 -> 20.0 mm, vias 0 -> 5
- net /ESP MCU/MEM_CS1: track 0.00 -> 15.1 mm
- net +3V3: track 0.00 -> 11.8 mm, vias 0 -> 5
- net Net-(D1-A): track 0.00 -> 11.4 mm
- net /ESP MCU/MEM_CLK: track 0.00 -> 8.33 mm, vias 0 -> 1
- net /ESP MCU/MEM_D2: track 0.00 -> 8.12 mm, vias 0 -> 1
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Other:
- board size 47 x 41.8 mm -> 47 x 47 mm
- board text added: "BOOT"
- board text added: "GND"
- board text added: "RESET"
- board text added: "TX RX"
